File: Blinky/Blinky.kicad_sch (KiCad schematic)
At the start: 60 parts, among them J1 Conn_01x06_Socket, J2 Conn_01x06_Socket, J3 Battery Connector, J4 Charging Notches, Q1 IRLML6244, Q2 IRLML6244, Q3 IRLML6244, Q4 IRLML6244, Q5 IRLML6244, Q6 IRLML6244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

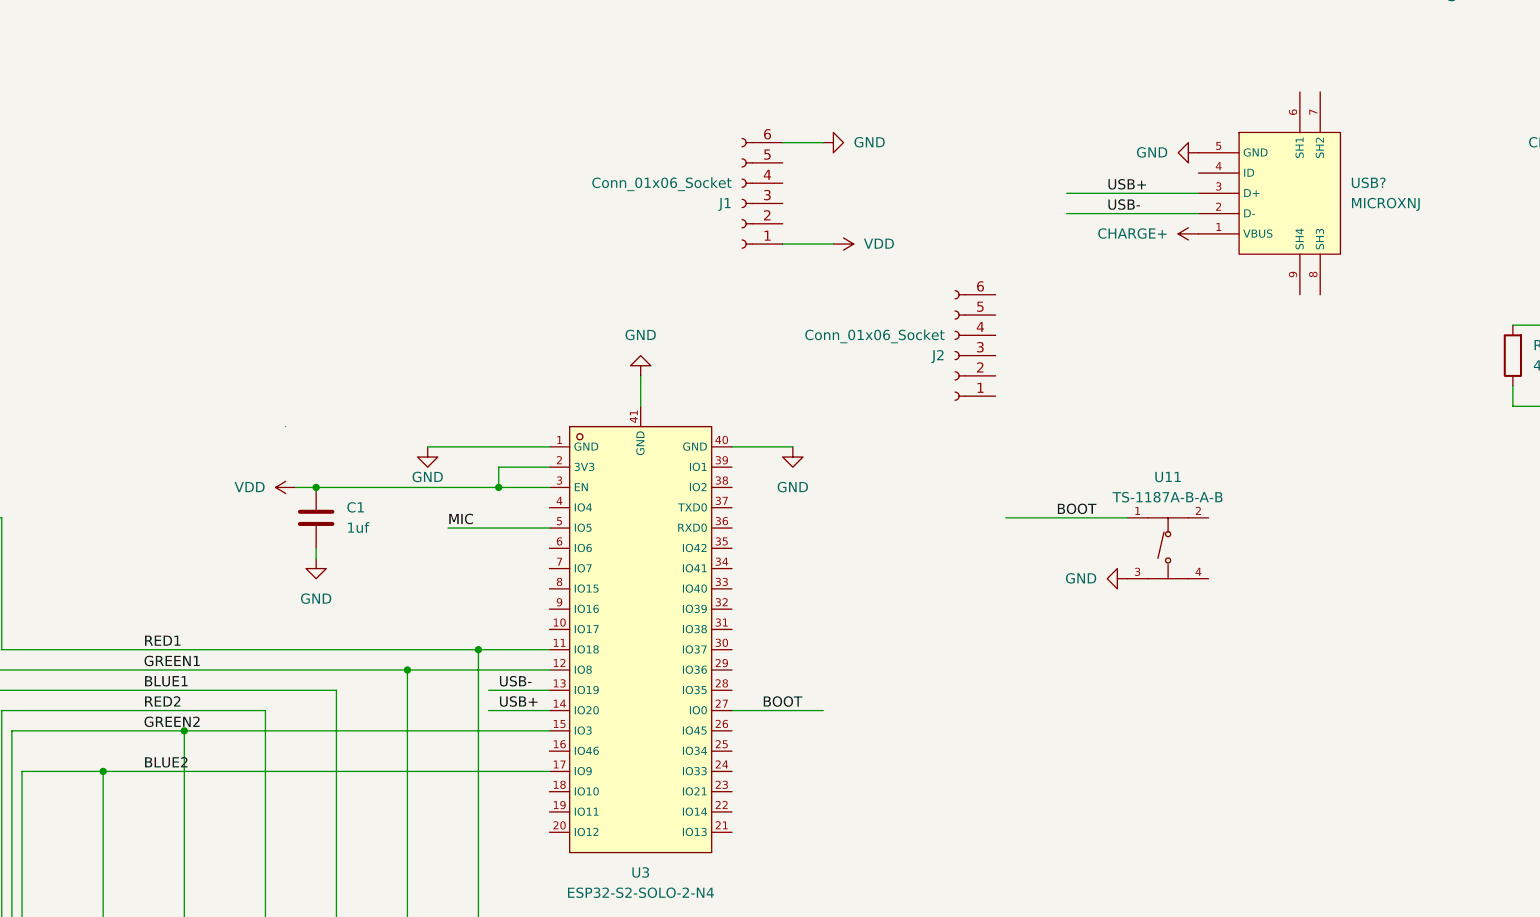
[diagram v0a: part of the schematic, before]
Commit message: connected pin headers to GPIOs
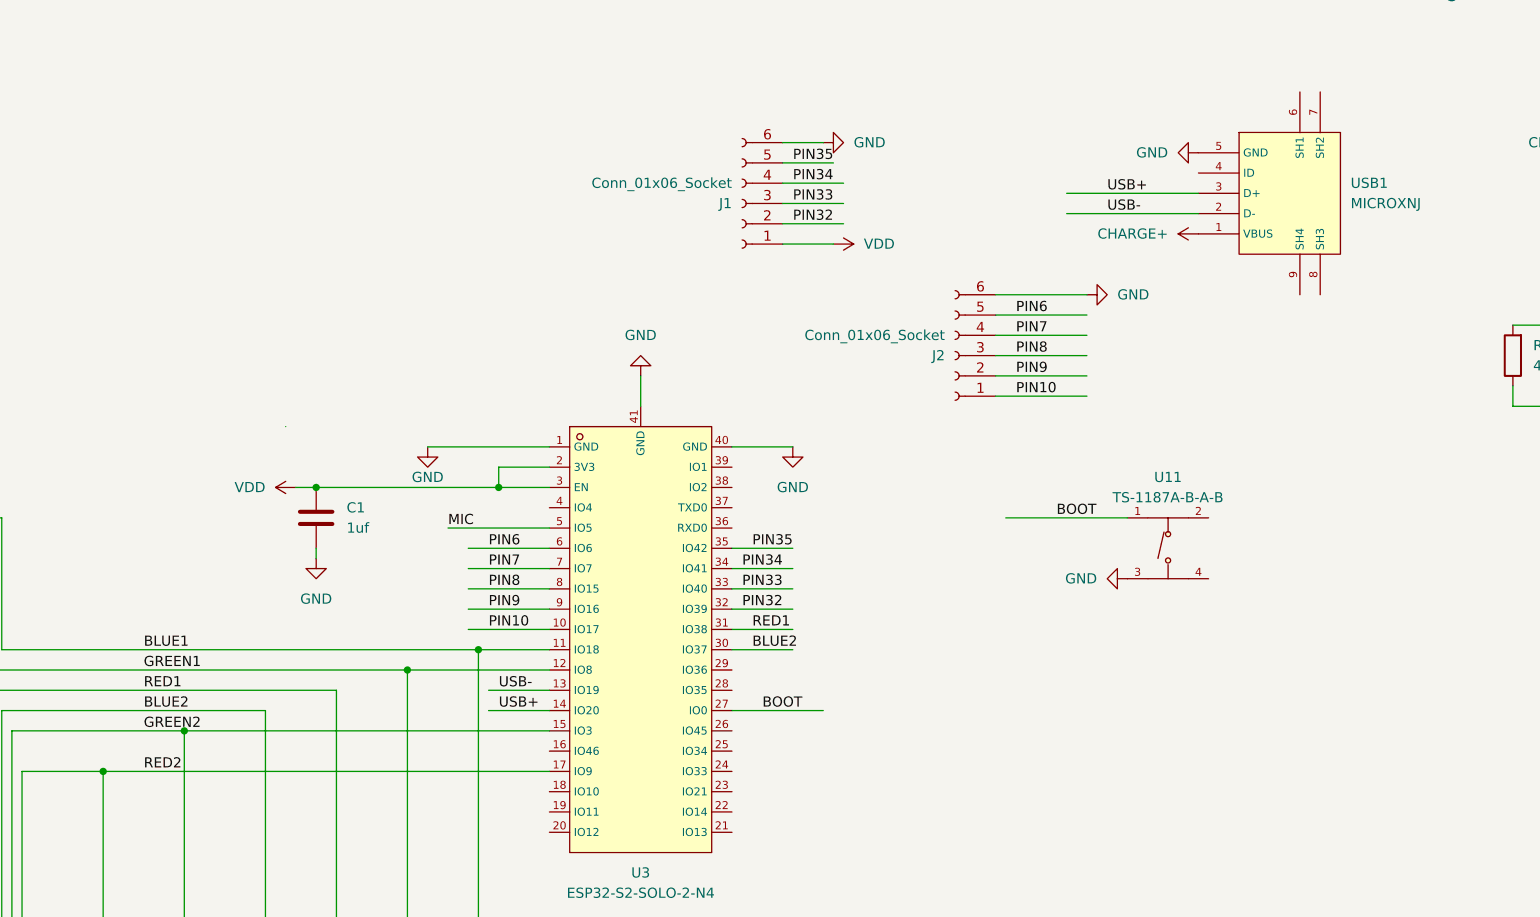
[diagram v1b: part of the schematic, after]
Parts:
- gave numbers to parts that had none: 1
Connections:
- net BLUE1: now also R18.2, R8.2, U3.11 (IO18); no longer R12.2, R16.2
- net BLUE2: now also R15.2, R6.2, U3.30 (IO37); no longer R13.2, R2.2, U3.17 (IO9)
- net GND: now also J2.6 (Pin_6)
- net RED1: now also R12.2, R16.2, U3.31 (IO38); no longer R18.2, R8.2, U3.11 (IO18)
- net RED2: now also R13.2, R2.2, U3.17 (IO9); no longer R15.2, R6.2
- net PIN32: now reaches J1.2 (Pin_2)
- net PIN32: now also U3.32 (IO39)
- net PIN33: now reaches J1.3 (Pin_3)
- net PIN33: now also U3.33 (IO40)
- net PIN34: now reaches J1.4 (Pin_4)
- net PIN34: now also U3.34 (IO41)
- net PIN35: now reaches J1.5 (Pin_5)
- net PIN35: now also U3.35 (IO42)
- net PIN10: now reaches J2.1 (Pin_1)
- net PIN10: now also U3.10 (IO17)
- net PIN9: now reaches J2.2 (Pin_2)
- net PIN9: now also U3.9 (IO16)
- net PIN8: now reaches J2.3 (Pin_3)
- net PIN8: now also U3.8 (IO15)
- net PIN7: now reaches J2.4 (Pin_4)
- net PIN7: now also U3.7 (IO7)
- net PIN6: now reaches J2.5 (Pin_5)
- net PIN6: now also U3.6 (IO6)

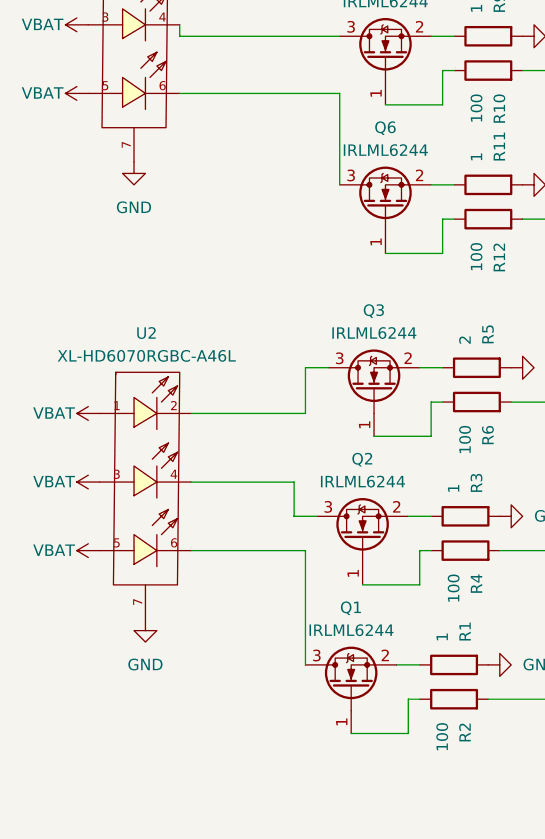
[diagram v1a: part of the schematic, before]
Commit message: removed ground connection for LED backside, added flipside led copper
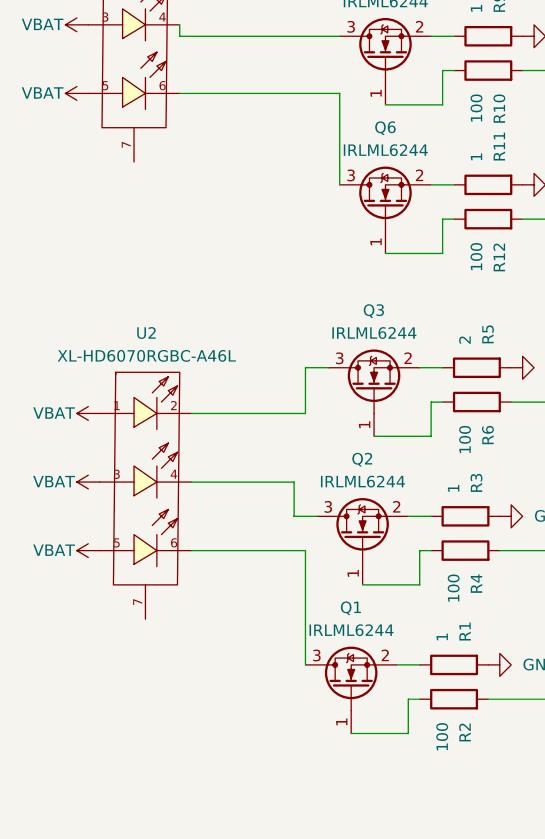
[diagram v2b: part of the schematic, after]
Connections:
- net GND: no longer U1.7, U2.7
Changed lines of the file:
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@@
-    )
-  )
-  (symbol (lib_id "power:GND") (at 67.31 198.12 0) (unit 1)
-    (in_bom yes) (on_board yes) (dnp no) (fields_autoplaced)
-    (property "Reference" "#PWR08" (at 67.31 204.47 0)
-      (effects (font (size 1.27 1.27)) hide)
-    )
-    (property "Value" "GND" (at 67.31 203.2 0)
-      (effects (font (size 1.27 1.27)))
-    )
-    (property "Footprint" "" (at 67.31 198.12 0)
-      (effects (font (size 1.27 1.27)) hide)
-    )
-    (property "Datasheet" "" (at 67.31 198.12 0)
-      (effects (font (size 1.27 1.27)) hide)
-    )
-    (pin "1")
-    (instances
-      (project "Blinky"
-        (path "/a854b35b-60aa-44a5-a34e-fbb2d526cb93"
-          (reference "#PWR08") (unit 1)
-        )
-      )
     )
   )
@@
         )
       )
-    )
-  )
-  (symbol (lib_id "power:GND") (at 66.04 147.32 0) (unit 1)
-    (in_bom yes) (on_board yes) (dnp no) (fields_autoplaced)
-    (property "Reference" "#PWR07" (at 66.04 153.67 0)
-      (effects (font (size 1.27 1.27)) hide)
-    )
-    (property "Value" "GND" (at 66.04 152.4 0)
-      (effects (font (size 1.27 1.27)))
-    )
-    (property "Footprint" "" (at 66.04 147.32 0)
-      (effects (font (size 1.27 1.27)) hide)
-    )
-    (property "Datasheet" "" (at 66.04 147.32 0)
-      (effects (font (size 1.27 1.27)) hide)
-    )
-    (pin "1")
-    (instances
-      (project "Blinky"
-        (path "/a854b35b-60aa-44a5-a34e-fbb2d526cb93"
-          (reference "#PWR07") (unit 1)
-        )
-      )

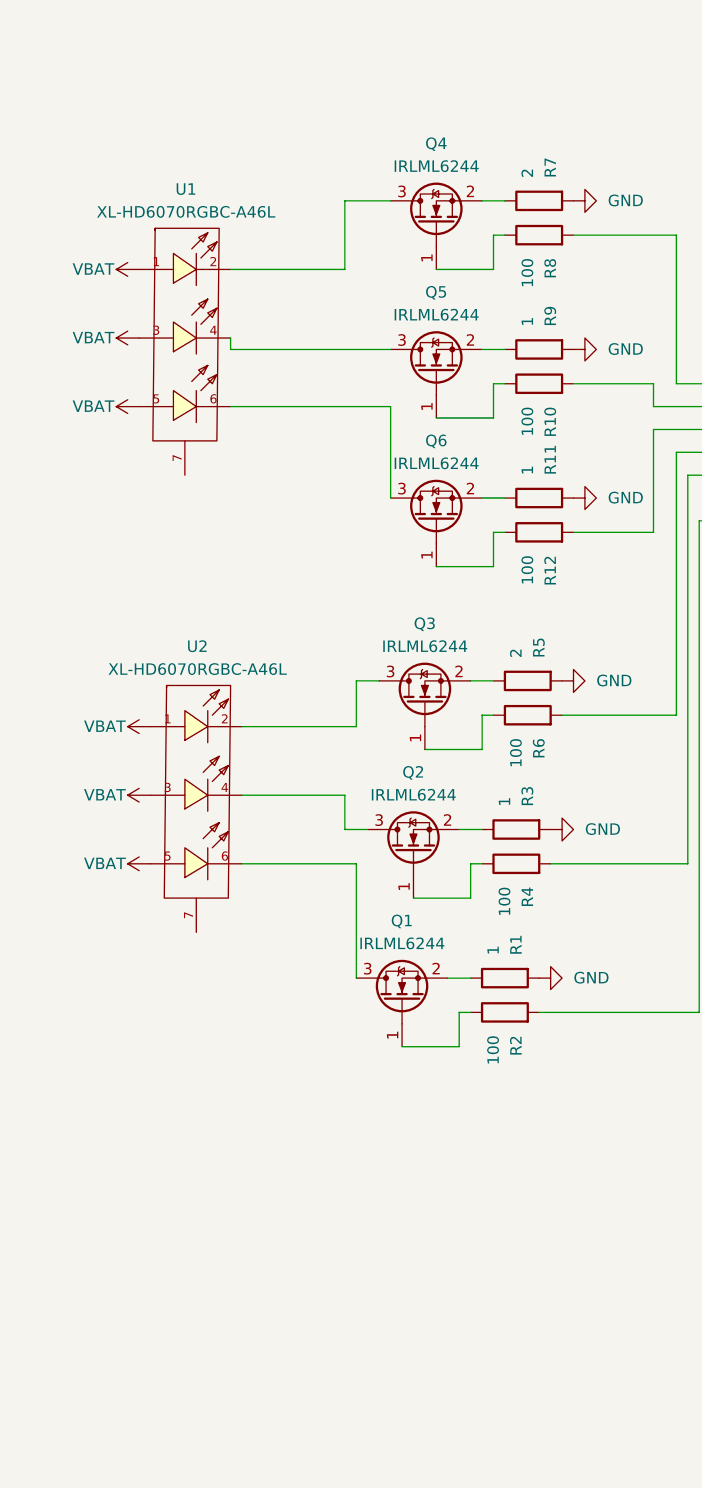
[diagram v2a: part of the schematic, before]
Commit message: switched around resistors for LEDs
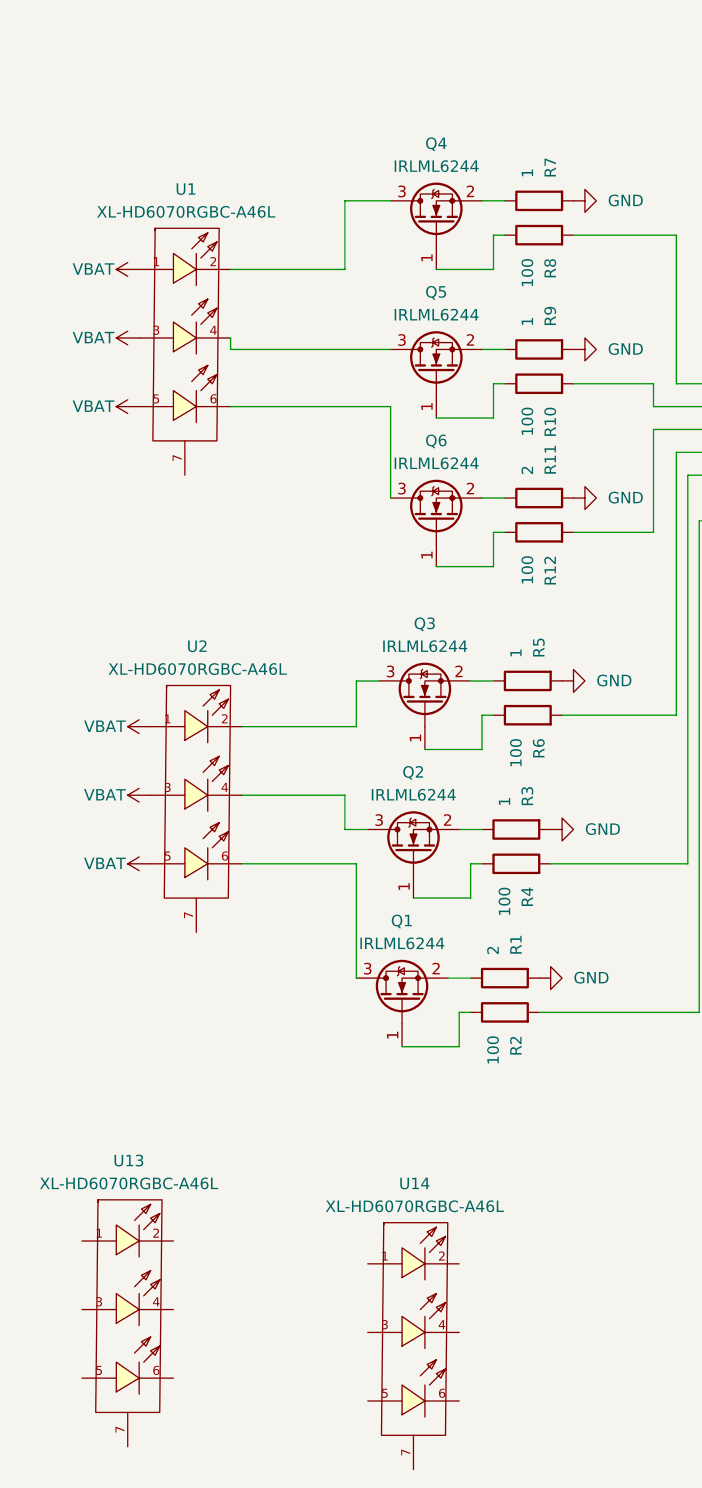
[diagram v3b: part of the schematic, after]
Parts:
- added U13, U14: XL-HD6070RGBC-A46L, footprint:LED-SMD_XL-HD6070RGBC-A46L-BACKSIDE, symbol XL-HD6070RGBC-A46L:XL-HD6070RGBC-A46L
- R1, R11: value 1 -> 2
- R5, R7: value 2 -> 1

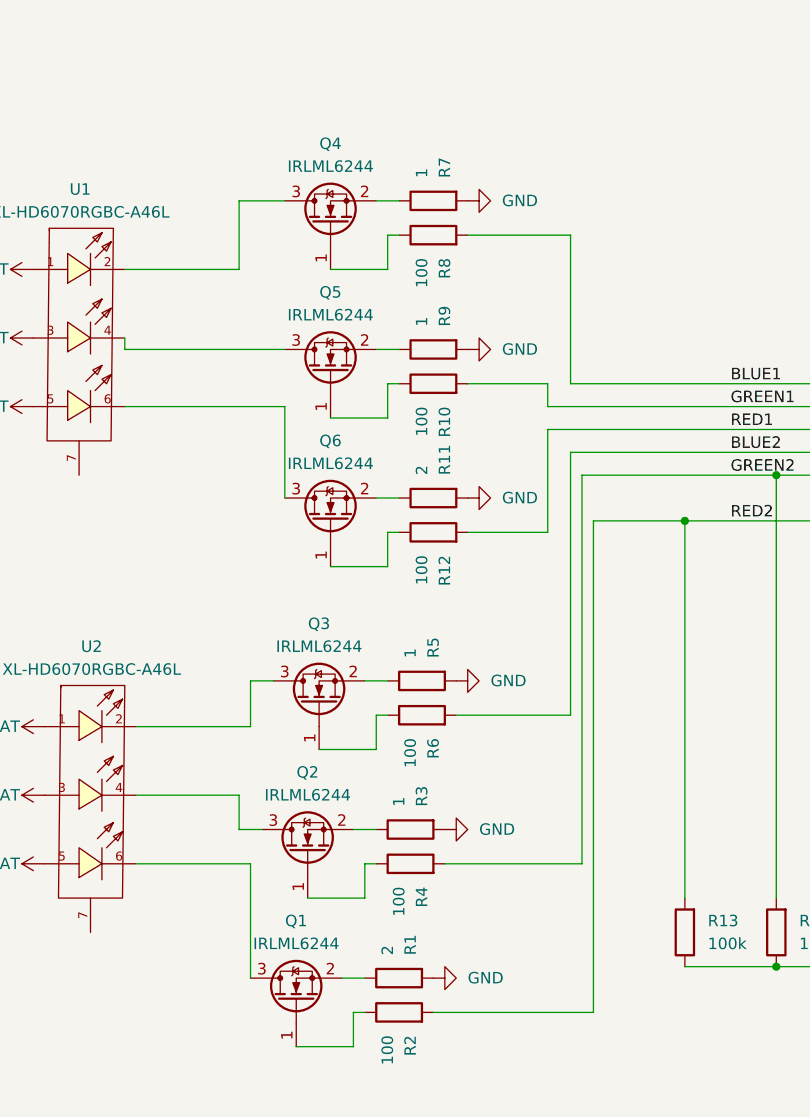
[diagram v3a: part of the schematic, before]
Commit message: doubled resistor values for LEDs
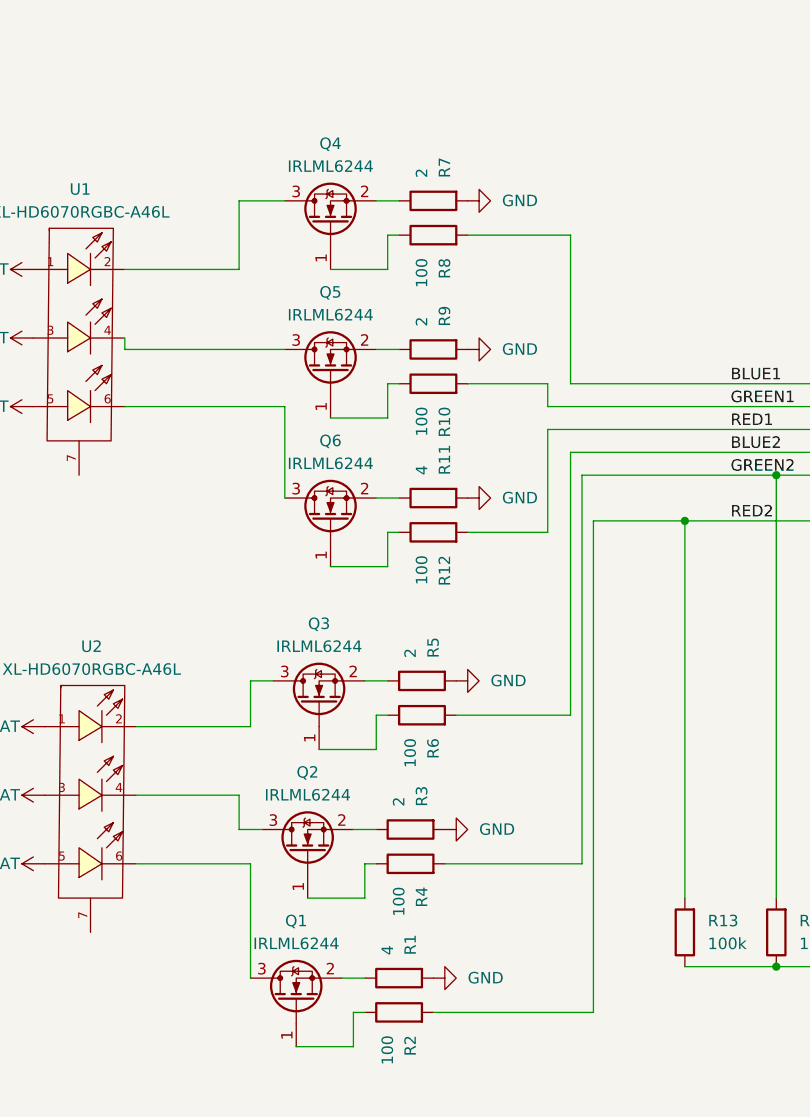
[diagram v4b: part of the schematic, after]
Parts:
- R1, R11: value 2 -> 4
- R3, R5, R7, R9: value 1 -> 2
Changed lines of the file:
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@@
       (effects (font (size 1.27 1.27)) (justify right))
     )
-    (property "Value" "1" (at 102.87 167.64 0)
+    (property "Value" "2" (at 102.87 167.64 0)
       (effects (font (size 1.27 1.27)) (justify right))
     )
@@
       (effects (font (size 1.27 1.27)) (justify right))
     )
-    (property "Value" "2" (at 100.33 200.66 0)
+    (property "Value" "4" (at 100.33 200.66 0)
       (effects (font (size 1.27 1.27)) (justify right))
     )
@@
       (effects (font (size 1.27 1.27)) (justify right))
     )
-    (property "Value" "2" (at 104.14 147.32 0)
+    (property "Value" "4" (at 104.14 147.32 0)
       (effects (font (size 1.27 1.27)) (justify right))
     )
@@
       (effects (font (size 1.27 1.27)) (justify right))
     )
-    (property "Value" "1" (at 101.6 184.15 0)
+    (property "Value" "2" (at 101.6 184.15 0)
       (effects (font (size 1.27 1.27)) (justify right))
     )
@@
       (effects (font (size 1.27 1.27)) (justify right))
     )
-    (property "Value" "1" (at 104.14 114.3 0)
+    (property "Value" "2" (at 104.14 114.3 0)
       (effects (font (size 1.27 1.27)) (justify right))
     )
@@
       (effects (font (size 1.27 1.27)) (justify right))
     )
-    (property "Value" "1" (at 104.14 130.81 0)
-      (effects (font (size 1.27 1.27)) (justify right))
-    )
+    (property "Value" "2" (at 104.14 130.81 0)
+      (effects (font (size 1.27 1.27)) (justify right))
+    )
